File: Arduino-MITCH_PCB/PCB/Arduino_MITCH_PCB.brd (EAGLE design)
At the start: 63.5 x 127 mm, 12 parts, among them J1 1725656

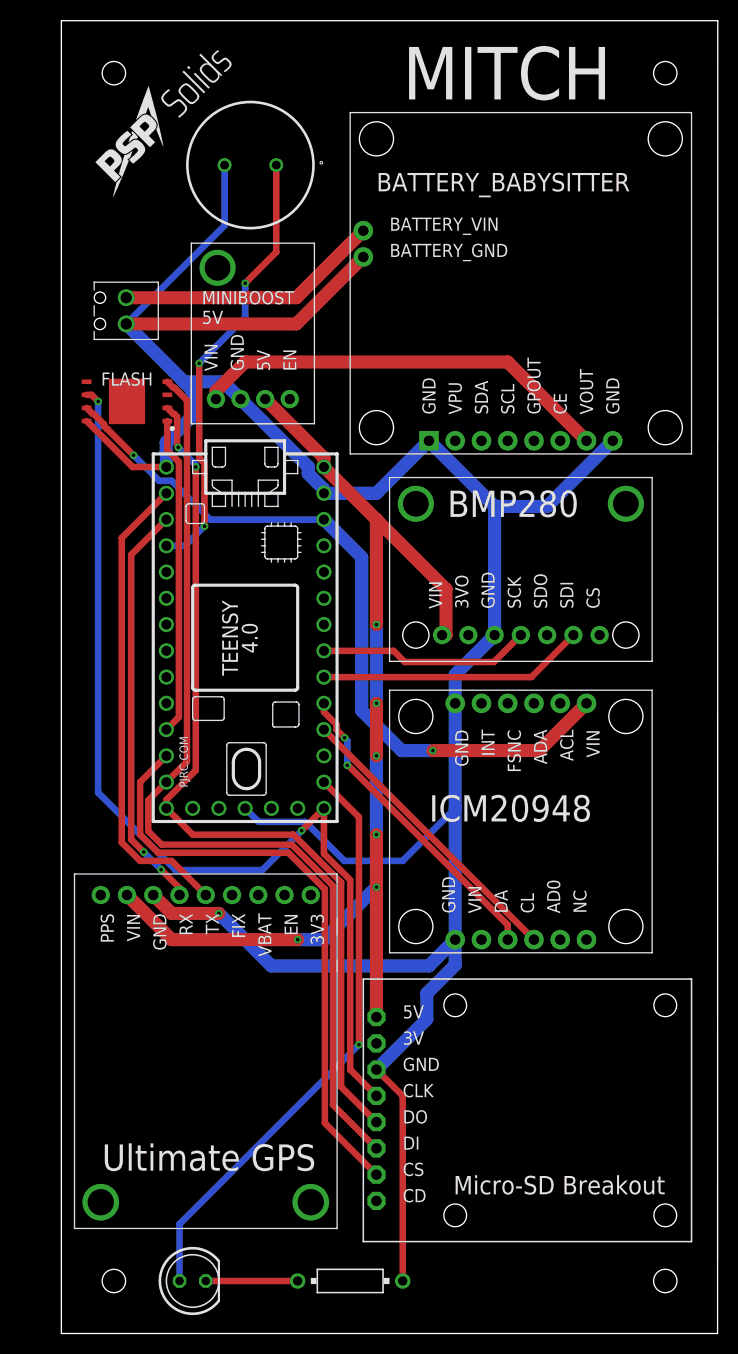
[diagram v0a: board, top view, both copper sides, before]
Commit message: Fixed Flash, added GND plane
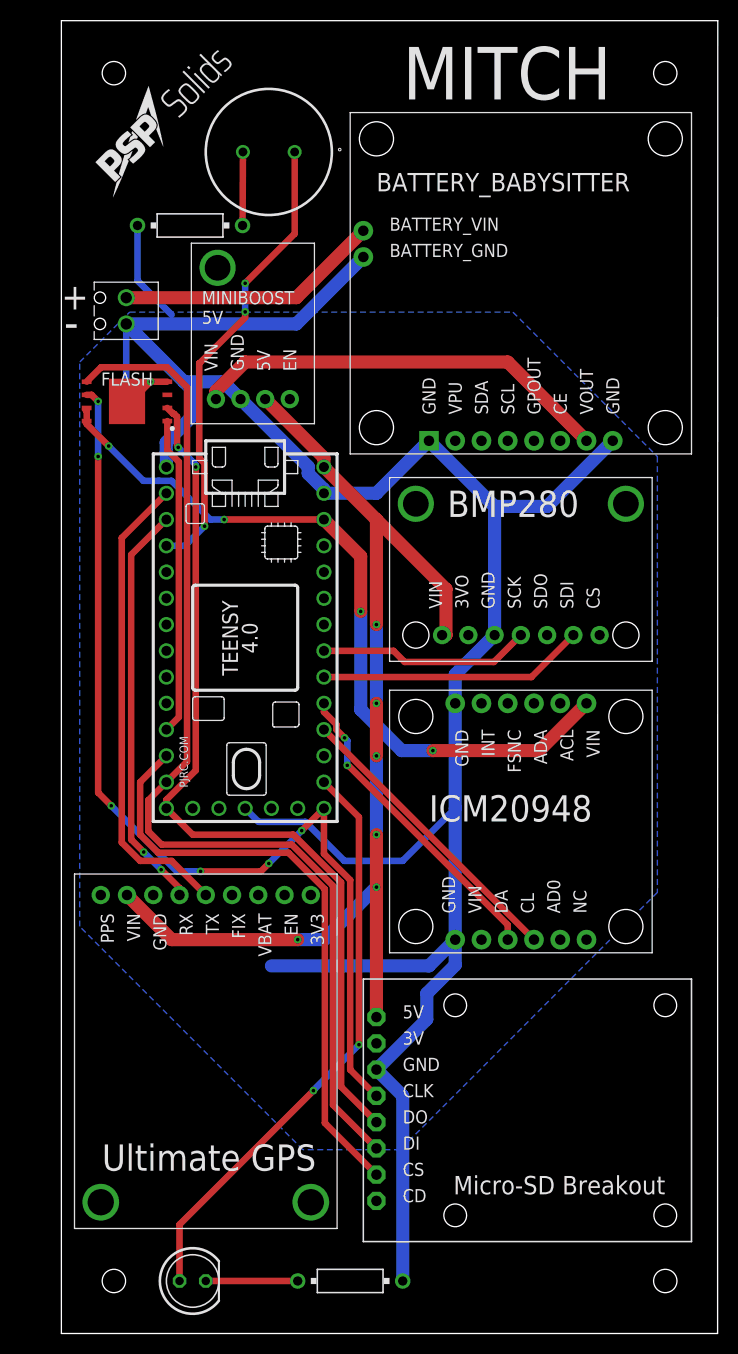
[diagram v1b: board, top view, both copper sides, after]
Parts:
- added R2: 220, resistor-power:HPS58
- R1: value 560 -> 220
- moved LS1 2.18 mm to (20.1, 114.3)
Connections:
- new net BUZZ-RES: LS1.2, R2.1
- net 3V3: now also FLASH.8; no longer FLASH.7
- net GND: now also FLASH.4, FLASH.9, R2.2; no longer FLASH.8, LS1.2
- net MOSI: now also FLASH.5; no longer FLASH.4
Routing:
- net GND: track 264.3 -> 244.2 mm
- net MOSI: track 93.1 -> 102.8 mm
- net BUZZ-RES: track 0.00 -> 7.11 mm
- net BUZZ: track 42.7 -> 44.7 mm
- net 3V3: track 72.8 -> 73.5 mm, vias 2 -> 4
- net SCK: track 96.6 -> 96.7 mm, vias 2 -> 6
- net LED: vias 1 -> 2
- added copper zone on layer 16, net GND
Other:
- board text added: "+"
- board text added: "-"

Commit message: Reshaped GND plane and completed drc
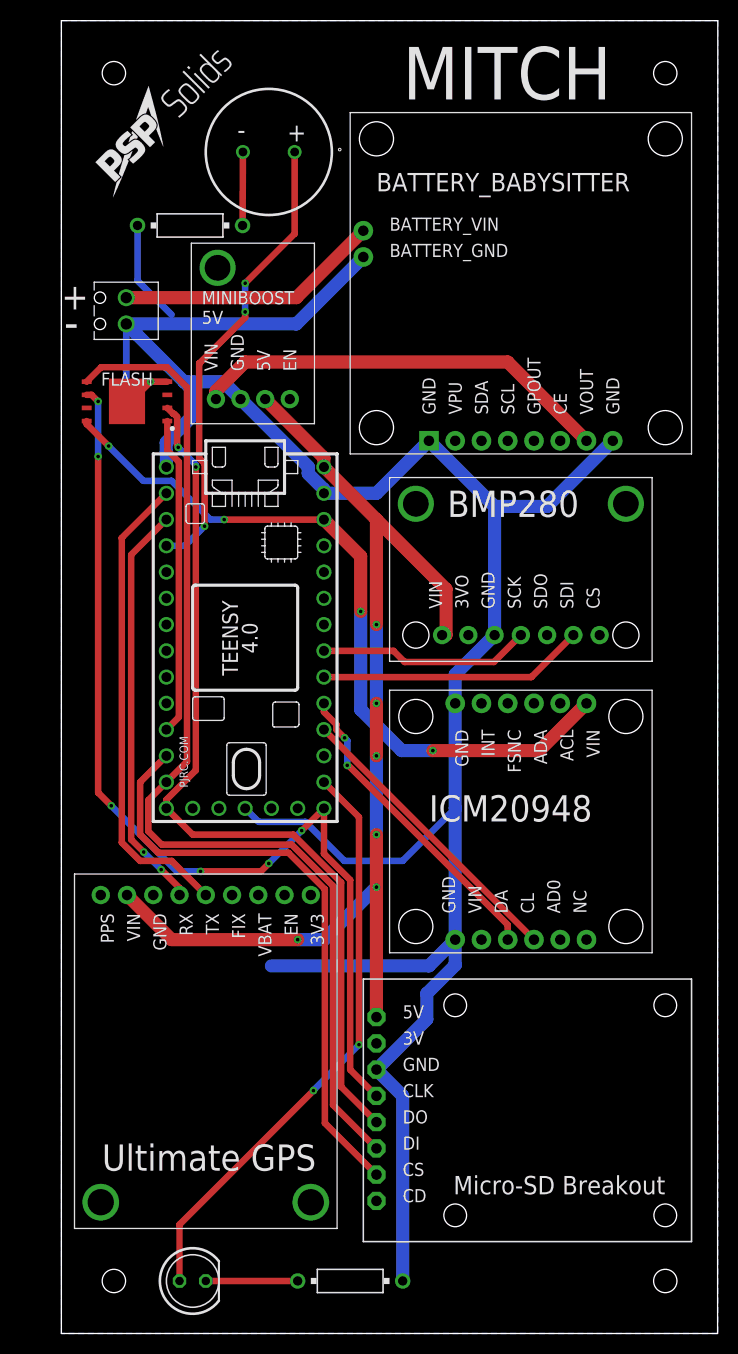
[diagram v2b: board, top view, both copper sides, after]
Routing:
- net 3V3: track 73.5 -> 72.3 mm
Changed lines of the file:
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@@
 <setting verticaltext="up"/>
 </settings>
-<grid distance="10" unitdist="mil" unit="mil" style="lines" multiple="1" display="yes" altdistance="5" altunitdist="mil" altunit="mil"/>
+<grid distance="10" unitdist="mil" unit="inch" style="lines" multiple="1" display="yes" altdistance="5" altunitdist="mil" altunit="mil"/>
 <layers>
 <layer number="1" name="Top" color="4" fill="1" visible="yes" active="yes"/>
@@
 <text x="0" y="99.06" size="2.54" layer="21">+</text>
 <text x="0.254" y="96.266" size="3.175" layer="21">-</text>
+<text x="21.844" y="115.316" size="1.778" layer="21">+</text>
+<text x="17.018" y="115.57" size="1.778" layer="21">-</text>
 </plain>
 <attributes>
@@
 <wire x1="6.275" y1="90.245" x2="6.35" y2="90.17" width="0.635" layer="16"/>
 <wire x1="10.25" y1="92.075" x2="8.636" y2="92.075" width="0.635" layer="1"/>
-<polygon width="0.254" layer="16">
-<vertex x="1.778" y="39.37"/>
-<vertex x="1.778" y="93.98"/>
-<vertex x="6.604" y="98.806"/>
-<vertex x="43.688" y="98.806"/>
-<vertex x="57.658" y="84.836"/>
-<vertex x="57.658" y="42.672"/>
-<vertex x="32.766" y="17.78"/>
-<vertex x="23.368" y="17.78"/>
-</polygon>
 <wire x1="6.731" y1="97.663" x2="6.275" y2="97.663" width="0.635" layer="16"/>
 <wire x1="33.02" y1="5.08" x2="33.02" y2="22.987" width="1.27" layer="16"/>
@@
 <wire x1="8.636" y1="92.075" x2="6.731" y2="90.17" width="0.635" layer="1"/>
 <wire x1="6.731" y1="90.17" x2="6.35" y2="90.17" width="0.635" layer="1"/>
+<polygon width="0.635" layer="16">
+<vertex x="0" y="127"/>
+<vertex x="63.5" y="127"/>
+<vertex x="63.5" y="0"/>
+<vertex x="0" y="0"/>
+</polygon>
 </signal>
 <signal name="BAT_VIN">
@@
 <contactref element="U$6" pad="VIN2"/>
 <contactref element="FLASH" pad="8"/>
-<wire x1="10.65975" y1="82.4865" x2="9.4279" y2="82.4865" width="0.635" layer="16"/>
 <wire x1="14.40625" y1="78.74" x2="10.65975" y2="82.4865" width="0.635" layer="16"/>
 <via x="35.941" y="56.388" extent="1-16" drill="0.35"/>
@@
 <wire x1="35.941" y1="56.388" x2="46.228" y2="56.388" width="1.27" layer="1"/>
 <wire x1="46.228" y1="56.388" x2="50.8" y2="60.96" width="1.27" layer="1"/>
-<wire x1="9.4279" y1="82.4865" x2="7.9375" y2="82.4865" width="0.635" layer="16"/>
+<wire x1="10.65975" y1="82.4865" x2="7.9375" y2="82.4865" width="0.635" layer="16"/>
 <wire x1="7.9375" y1="82.4865" x2="4.572" y2="85.852" width="0.635" layer="16"/>
 <via x="4.572" y="85.852" extent="1-16" drill="0.35"/>
 <wire x1="4.572" y1="85.852" x2="2.45" y2="87.974" width="0.635" layer="1"/>
-<wire x1="2.45" y1="87.974" x2="2.45" y2="88.265" width="0.635" layer="1"/>
 <wire x1="28.956" y1="60.3542625" x2="28.956" y2="69.85" width="1.27" layer="16"/>
 <via x="28.956" y="69.85" extent="1-16" drill="0.35"/>
@@
 <via x="15.748" y="78.74" extent="1-16" drill="0.35"/>
 <wire x1="15.748" y1="78.74" x2="14.40625" y2="78.74" width="0.635" layer="16"/>
-<wire x1="2.45" y1="88.265" x2="2.45" y2="89.244" width="0.635" layer="1"/>
-<wire x1="2.45" y1="89.244" x2="2.286" y2="89.408" width="0.635" layer="1"/>
+<wire x1="2.45" y1="87.974" x2="2.45" y2="88.265" width="0.635" layer="1"/>
 </signal>
 <signal name="SCL0">
